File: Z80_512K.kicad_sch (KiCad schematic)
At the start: 25 parts, among them J1 USB_B_Mini, J2 EXPANSION-BUS, SW1 ON|OFF, SW2 Z80-RESET, U1 Z84C00/PLCC, U2 74HC574, U3 512K-SRAM, U4 74HC138, U5 512K-EEPROM, U6 74HC74, U7 74HC00, Y1 20MHz-DIP14

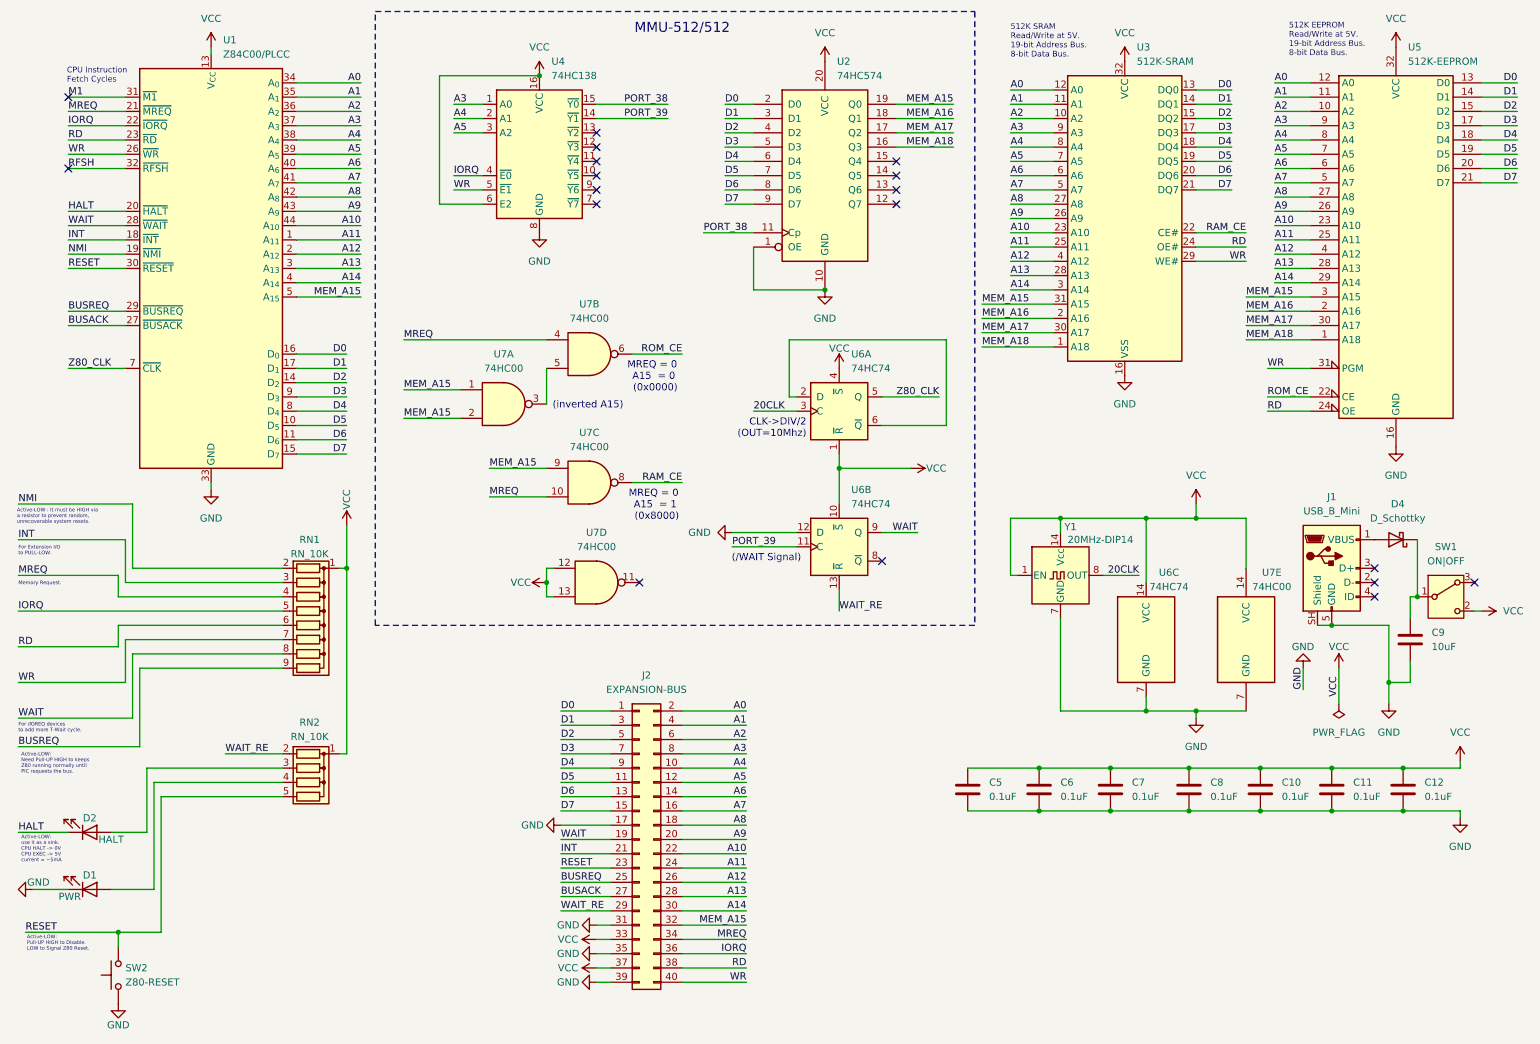
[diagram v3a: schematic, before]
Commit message: Rev1.1: fixed 74HC00/74 footprint, schematic(CE,Bus,574..), layout.
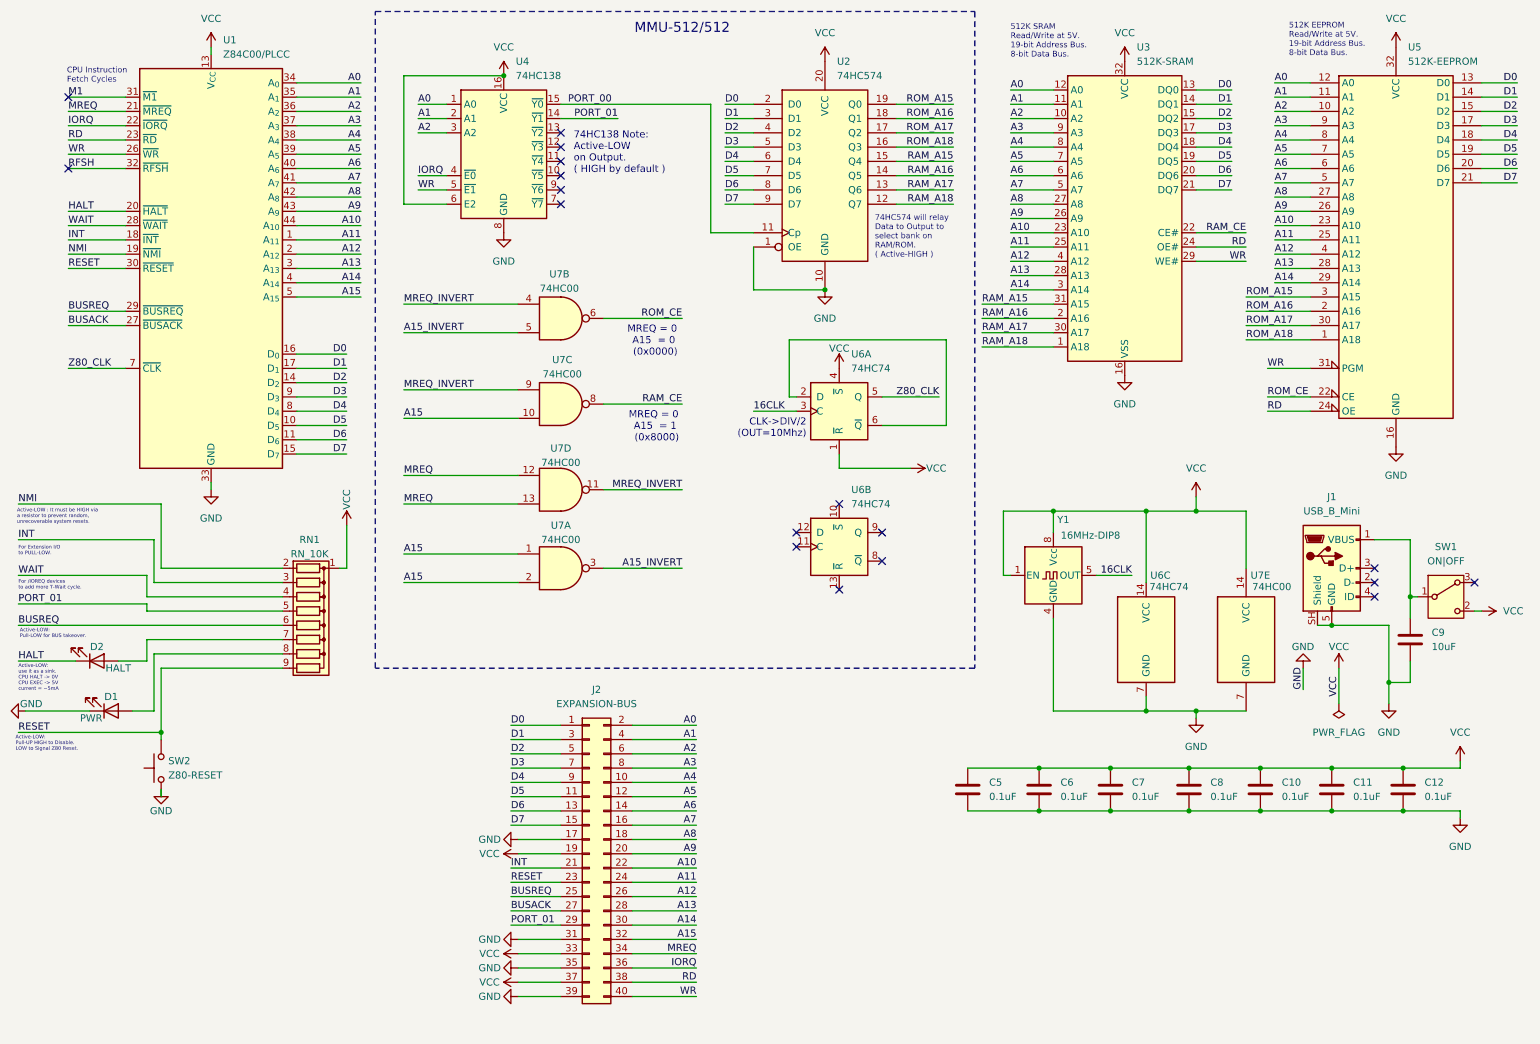
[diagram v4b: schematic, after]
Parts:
- removed D4: D_Schottky, Diode_THT:D_DO-41_SOD81_P10.16mm_Horizontal, symbol Device:D_Schottky
- removed RN2: RN_10K, Resistor_THT:R_Array_SIP5, symbol Device:R_Network04
- U6, U7: footprint Package_DIP:DIP-14_W10.16mm -> Package_DIP:DIP-14_W7.62mm
- Y1: value 20MHz-DIP14 -> 16MHz-DIP8; footprint Oscillator:Oscillator_DIP-14 -> Oscillator:Oscillator_DIP-8; symbol Oscillator:CXO_DIP14 -> Oscillator:CXO_DIP8
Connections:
- net A0: now also U4.1 (A0)
- net A1: now also U4.2 (A1)
- net A2: now also U4.3 (A2)
- net A3: no longer U4.1 (A0)
- net A4: no longer U4.2 (A1)
- net A5: no longer U4.3 (A2)
- net BUSREQ: now also RN1.6 (R5); no longer RN1.9 (R8)
- net GND: now also Y1.4 (GND); no longer U6.12 (D), Y1.7 (GND)
- net IORQ: no longer RN1.5 (R4)
- net MREQ: now also U7.12, U7.13; no longer RN1.4 (R3), U7.10, U7.4
- net RD: no longer RN1.6 (R5)
- net RESET: now also RN1.9 (R8)
- net VCC: now also J2.19 (Pin_19), Y1.8 (Vcc); no longer U6.10 (~{S}), U7.12, U7.13, Y1.14 (Vcc)
- net WAIT: now also RN1.4 (R3); no longer J2.19 (Pin_19), RN1.8 (R7), U6.9 (Q)
- net WR: no longer RN1.7 (R6)
- net at D1.2 (A): now also RN1.8 (R7)
- net A15_INVERT: now reaches U7.3, U7.5
- net MREQ_INVERT: now reaches U7.11
- net MREQ_INVERT: now also U7.4, U7.9
- net at D2.2 (A): now also RN1.7 (R6)
- net at J1.1 (VBUS): now also C9.2, SW1.1 (B)
- net RAM_A18: now reaches U2.12 (Q7)
- net RAM_A18: now also U3.1 (A18)
- net RAM_A17: now reaches U2.13 (Q6)
- net RAM_A17: now also U3.30 (A17)
- net RAM_A16: now reaches U2.14 (Q5)
- net RAM_A16: now also U3.2 (A16)
- net RAM_A15: now reaches U2.15 (Q4)
- net RAM_A15: now also U3.31 (A15)
- net 20CLK renamed 16CLK
- net 16CLK: now also Y1.5 (OUT); no longer Y1.8 (OUT)
- net MEM_A15 renamed A15
- net A15: now also U7.10; no longer U2.19 (Q0), U3.31 (A15), U5.3 (A15), U7.9
- net MEM_A16 renamed ROM_A16
- net ROM_A16: no longer U3.2 (A16)
- net MEM_A17 renamed ROM_A17
- net ROM_A17: no longer U3.30 (A17)
- net MEM_A18 renamed ROM_A18
- net ROM_A18: no longer U3.1 (A18)
- net PORT_38 renamed PORT_00
- net PORT_39: no longer names the net of U6.11 (C)
- net PORT_39: no longer U4.14 (~{Y1})
- net WAIT_RE: no longer names the net of U6.13 (~{R})
- net WAIT_RE: no longer J2.29 (Pin_29)
- new net PORT_01: J2.29 (Pin_29), RN1.5 (R4), U4.14 (~{Y1})
- new net ROM_A15: U2.19 (Q0), U5.3 (A15)
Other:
- note added: "74HC138 Note: Active-LOW on Output. ( HIGH by default )"
- note added: "74HC574 will relay Data to Output to select bank on RAM/ROM. ( Active-HIGH )"
- note added: "Active-LOW: Pull-LOW for BUS takeover."
- note removed: "(/WAIT Signal)"
- note removed: "(inverted A15)"
- note removed: "Active-LOW: Need Pull-UP HIGH to keeps Z80 running normally until PIC requests the bus."
- note removed: "Memory Request."
- moved on the sheet: D1, D2, J2, SW2, U4, U7A, U7B, U7C, U7D, Y1

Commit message: Add 1xCap + adjust closer->74HC74.
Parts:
- added C13: 0.1uF, Capacitor_THT:C_Disc_D3.4mm_W2.1mm_P2.50mm, symbol Device:C
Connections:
- net GND: now also C13.1
- net VCC: now also C13.2

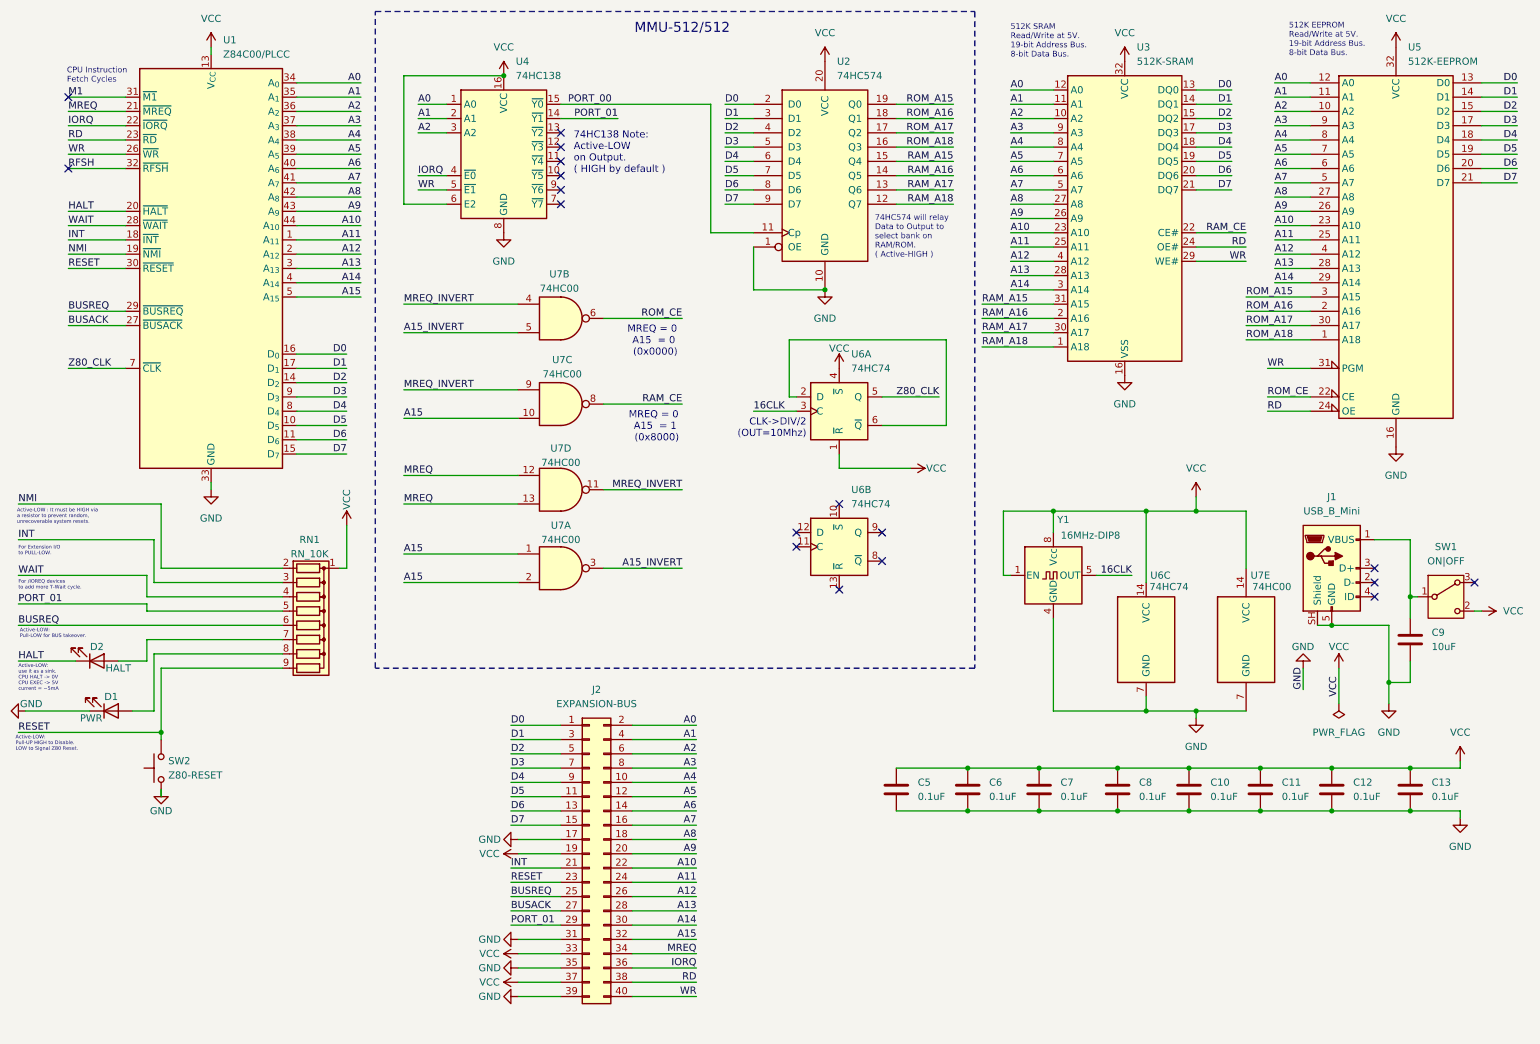
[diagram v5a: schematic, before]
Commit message: Rev1.2: Update on Data Latch w/ Flip-Flop
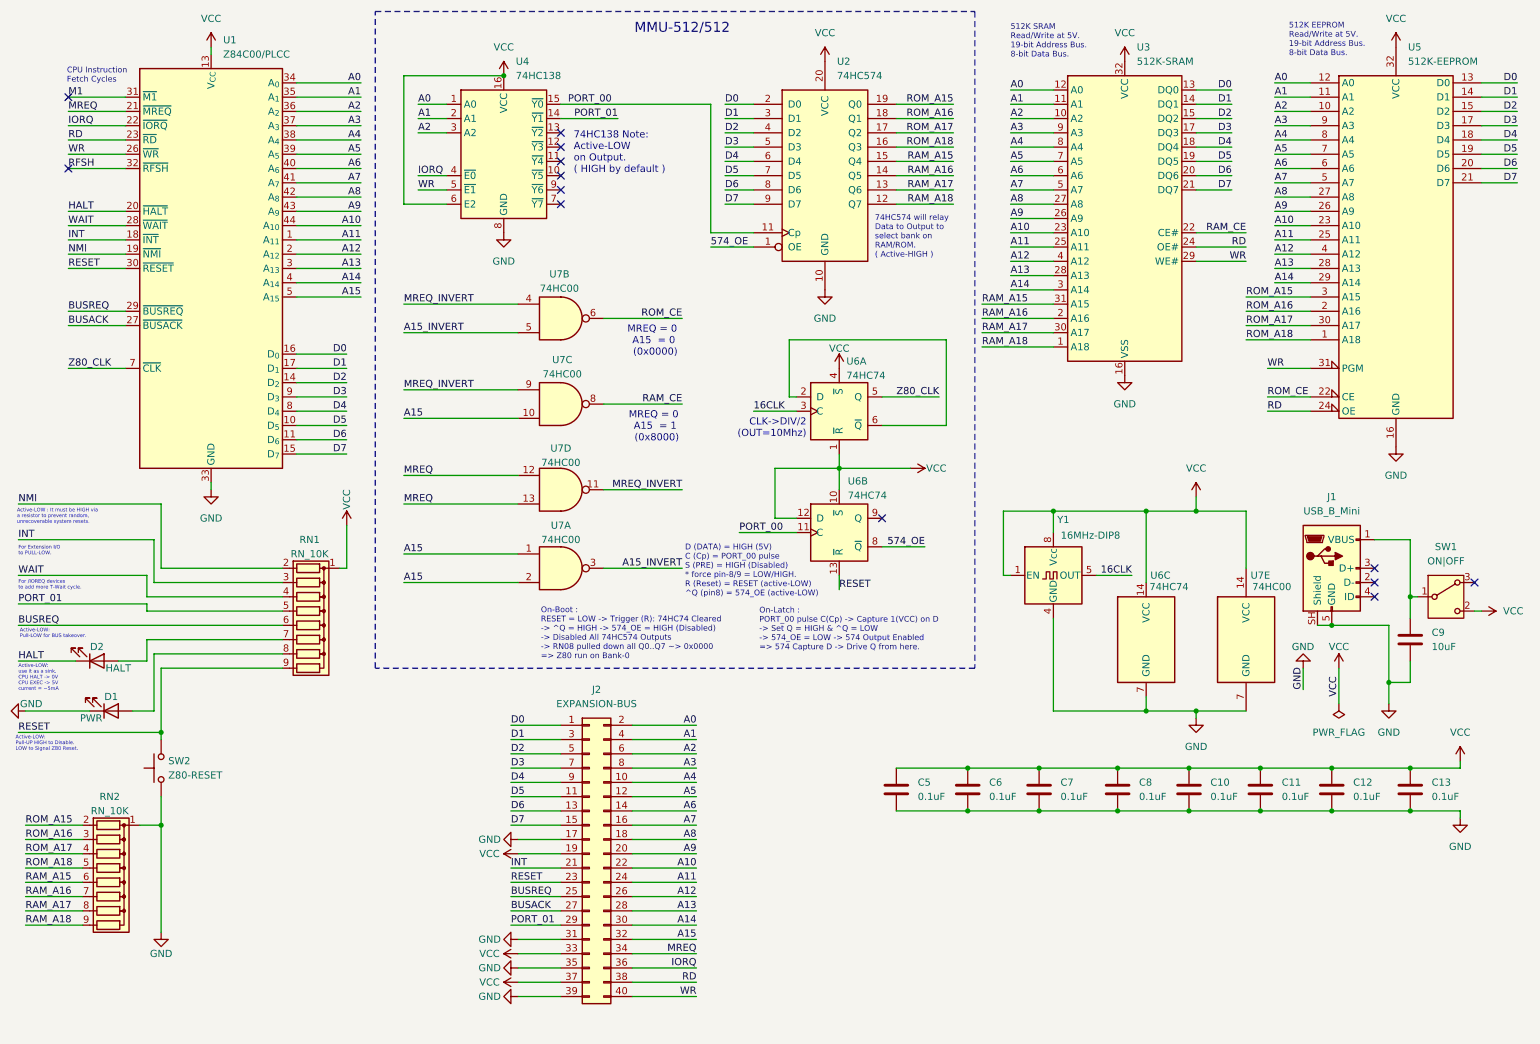
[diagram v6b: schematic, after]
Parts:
- added RN2: RN_10K, Resistor_THT:R_Array_SIP9, symbol Device:R_Network08
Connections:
- net GND: now also RN2.1 (common); no longer U2.1 (OE)
- net PORT_00: now also U6.11 (C)
- net RAM_A15: now also RN2.6 (R5)
- net RAM_A16: now also RN2.7 (R6)
- net RAM_A17: now also RN2.8 (R7)
- net RAM_A18: now also RN2.9 (R8)
- net RESET: now also U6.13 (~{R})
- net ROM_A15: now also RN2.2 (R1)
- net ROM_A16: now also RN2.3 (R2)
- net ROM_A17: now also RN2.4 (R3)
- net ROM_A18: now also RN2.5 (R4)
- net VCC: now also U6.10 (~{S}), U6.12 (D)
- net 574_OE: now reaches U6.8 (~{Q})
- net 574_OE: now also U2.1 (OE)
- no-connect marks 18 -> 13
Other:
- note added: "D (DATA) = HIGH (5V) C (Cp) = PORT_00 pulse S (PRE) = HIGH (Disabled) * force pin-8/9 = LOW/HIGH. R (Reset) = RESET (active-LOW) ^Q (pin8) = 574_OE (active-LOW)"
- note added: "On-Boot : RESET = LOW -> Trigger (R): 74HC74 Cleared -> ^Q = HIGH -> 574_OE = HIGH (Disabled) -> Disabled All 74HC574 Outputs -> RN08 pulled down all Q0..Q7 ~> 0x0000 => Z80 run on Bank-0"
- note added: "On-Latch : PORT_00 pulse C(Cp) -> Capture 1(VCC) on D -> Set Q = HIGH & ^Q = LOW -> 574_OE = LOW -> 574 Output Enabled => 574 Capture D -> Drive Q from here."
- moved on the sheet: U6B

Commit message: Rev1.2: Fix 74HC574/74 for Bank0.
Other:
- note added: "RAM/ROM default Bank ~> 0 By Pull-Down all Outputs from 74HC574."
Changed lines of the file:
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@@
+		)
+	)
+	(text "RAM/ROM default Bank ~> 0\nBy Pull-Down all Outputs\nfrom 74HC574."
+		(exclude_from_sim no)
+		(at 41.91 161.544 0)
+		(effects
+			(font
+				(size 1.016 1.016)
+			)
+			(justify left)
 		)
 	)

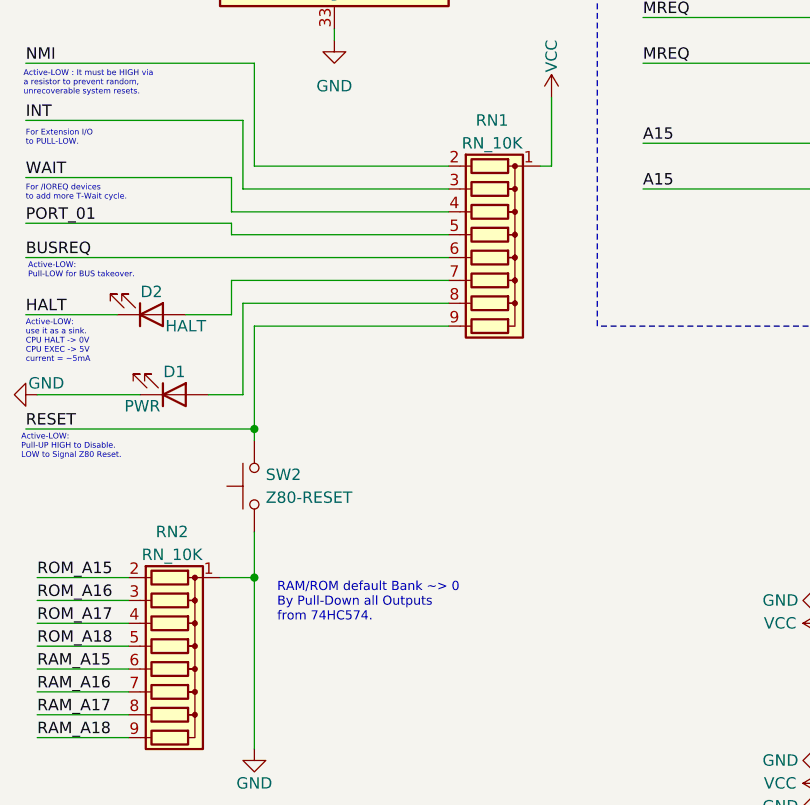
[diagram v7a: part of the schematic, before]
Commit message: Rev1.2.1: refine RESET circuit.
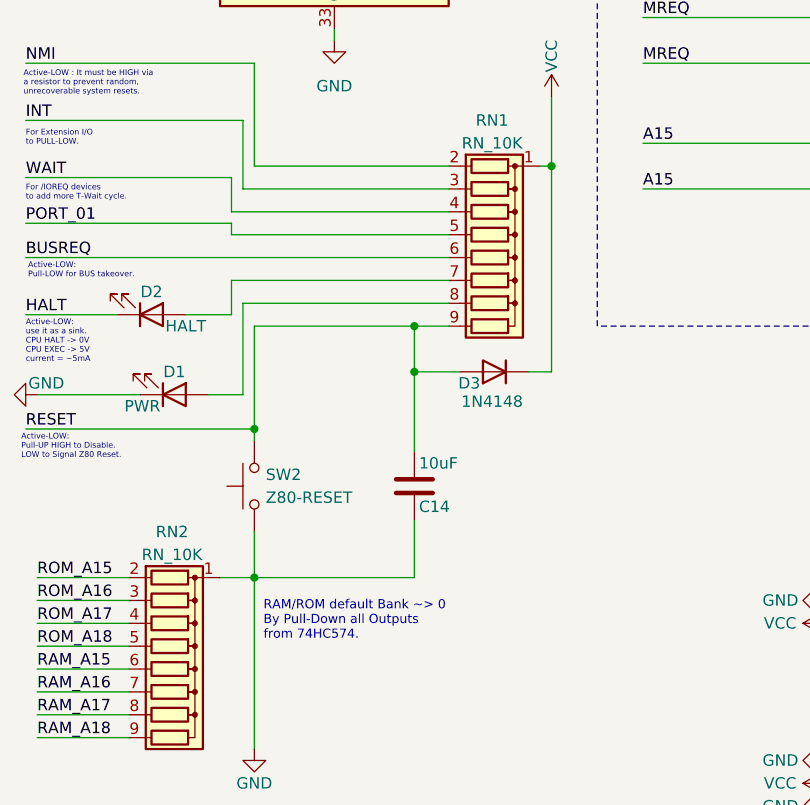
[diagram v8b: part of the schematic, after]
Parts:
- added C14: 10uF, Capacitor_THT:C_Radial_D4.0mm_H5.0mm_P1.50mm, symbol Device:C
- added D3: 1N4148, Diode_THT:D_DO-35_SOD27_P7.62mm_Horizontal, symbol Diode:1N4148
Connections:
- net GND: now also C14.2
- net RESET: now also C14.1, D3.2 (A)
- net VCC: now also D3.1 (K)
